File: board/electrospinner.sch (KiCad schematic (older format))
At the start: 40 parts, among them J1 12Vin, J2 Programmer, J3 MotorConnector, J4 TempSensor, J5 USB_B, SW1 ResetBTN, U1 TPS62147, U2 FT230XS, U3 MSP430G2553IPW20

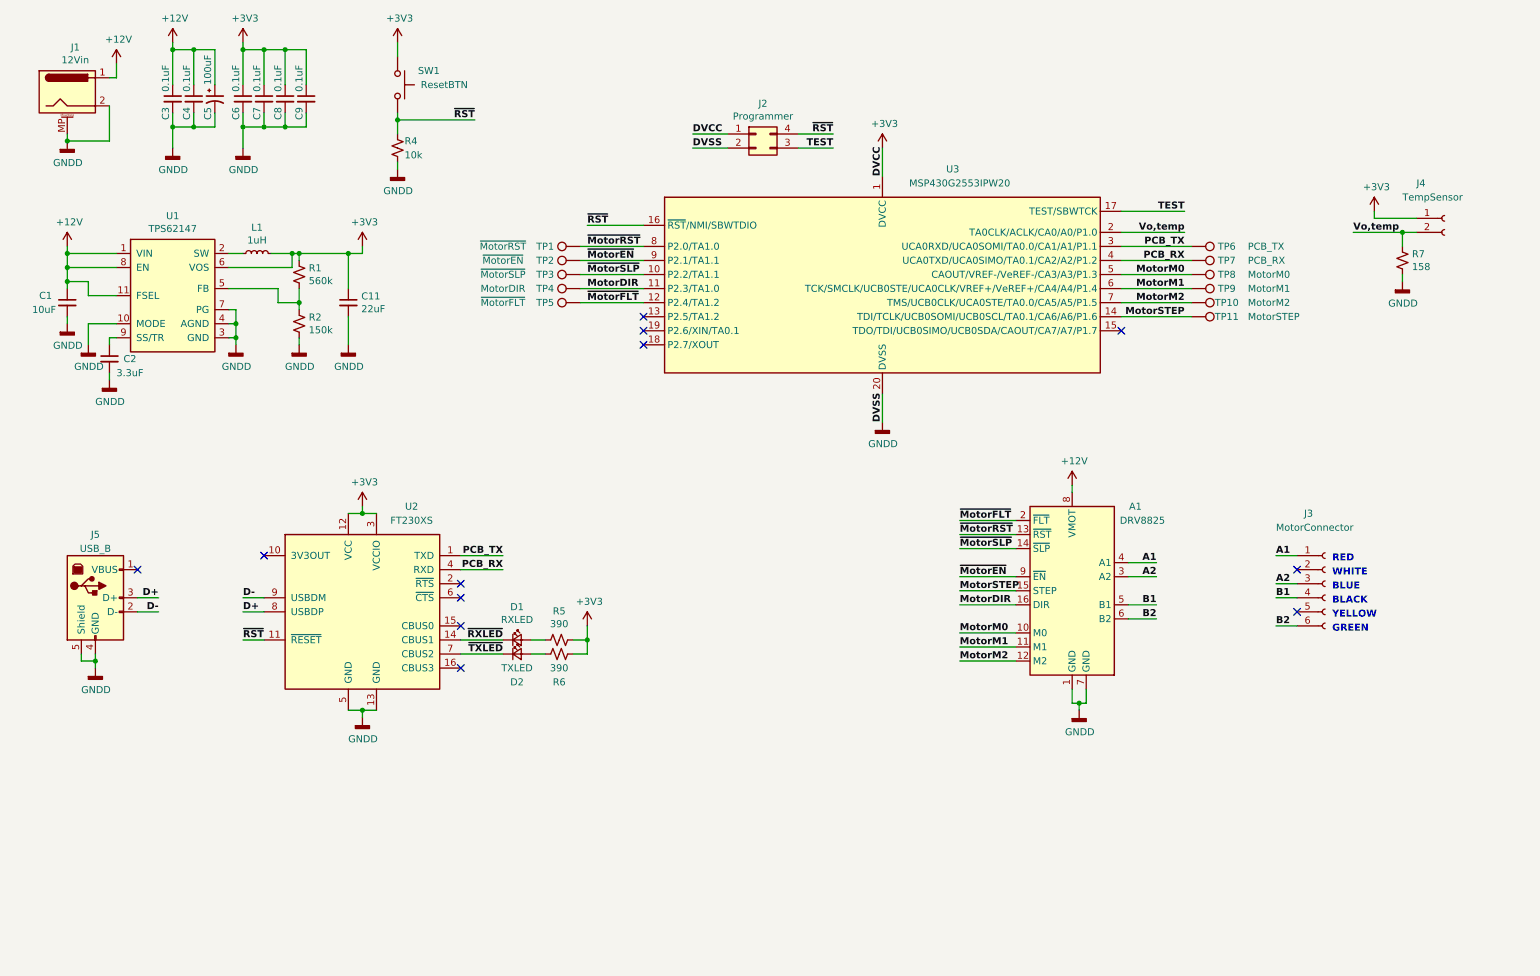
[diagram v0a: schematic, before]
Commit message: Re-updates rev5 files
Adds labels to schematic
Renames uart.pdf to usb_to_uart.pdf
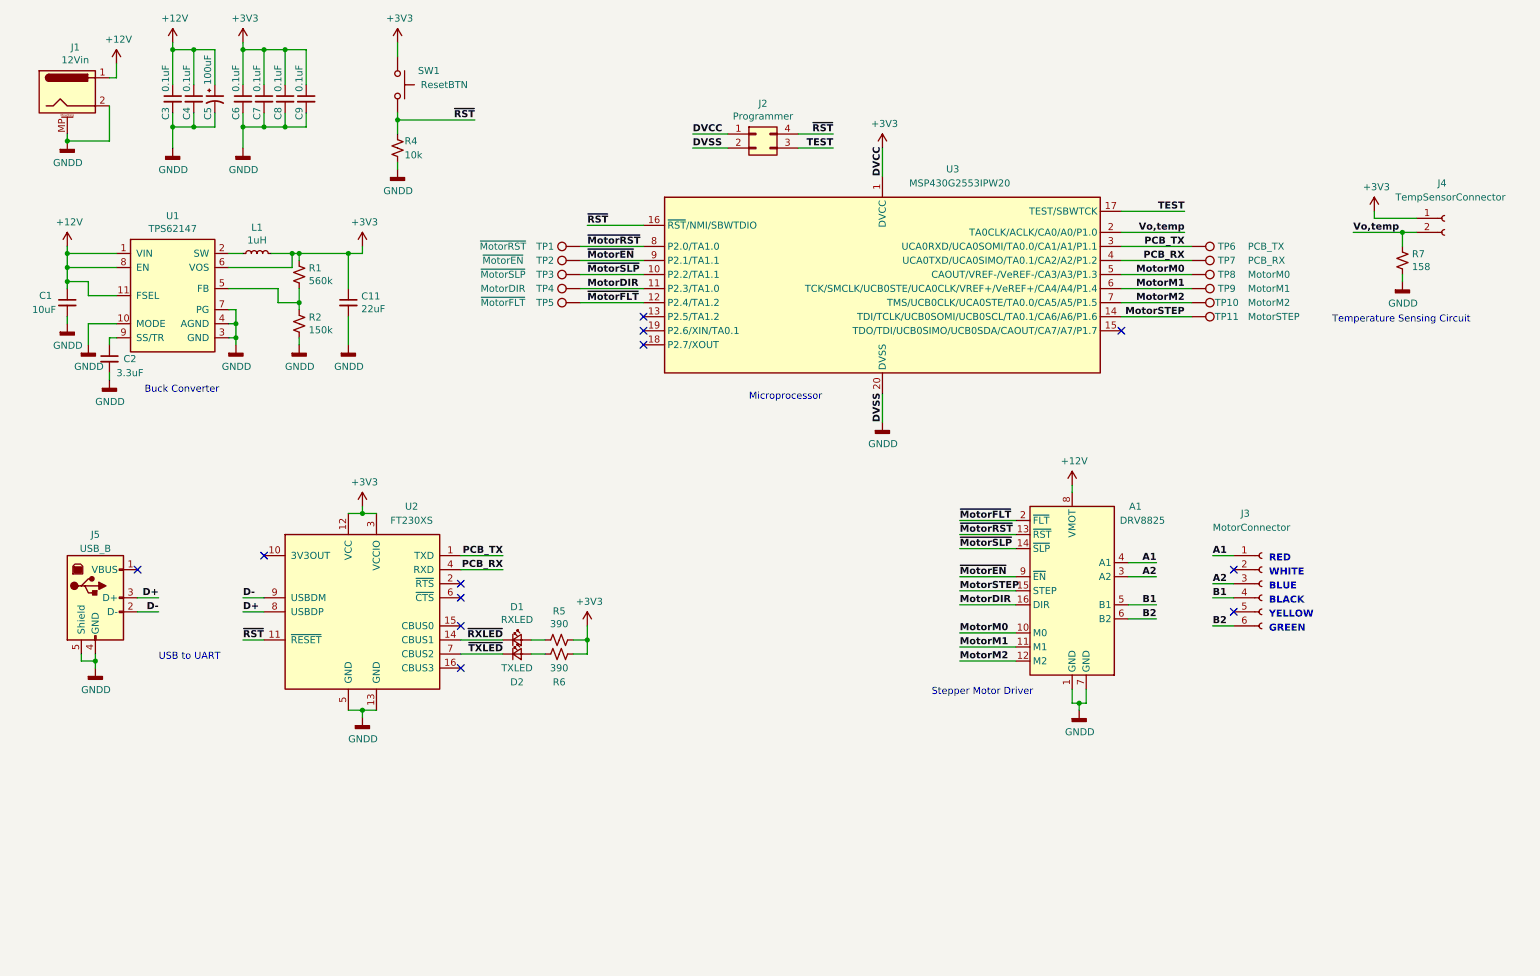
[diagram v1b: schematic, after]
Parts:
- J4: value TempSensor -> TempSensorConnector
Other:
- note added: "Buck Converter"
- note added: "Microprocessor"
- note added: "Stepper Motor Driver"
- note added: "Temperature Sensing Circuit"
- note added: "USB to UART"
- moved on the sheet: J3
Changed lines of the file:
@@
 L electrospinner-rescue:Conn_01x06_Female-Connector J3
 U 1 1 5C96304A
-P 9850 4550
-F 0 "J3" H 9700 5050 50  0000 L CNN
-F 1 "MotorConnector" H 9500 4950 50  0000 L CNN
-F 2 "Connector_JST:JST_XH_B6B-XH-AM_1x06_P2.50mm_Vertical" H 9850 4550 50  0001 C CNN
-F 3 "~" H 9850 4550 50  0001 C CNN
-F 4 "resource-center" H 2650 -850 50  0001 C CNN "Status"
-	1    9850 4550
-	1    0    0    -1
-$EndComp
-NoConn ~ 9650 4750
-NoConn ~ 9650 4450
-Text Label 9500 4850 0    50   ~ 10
+P 9400 4550
+F 0 "J3" H 9250 5050 50  0000 L CNN
+F 1 "MotorConnector" H 9050 4950 50  0000 L CNN
+F 2 "Connector_JST:JST_XH_B6B-XH-AM_1x06_P2.50mm_Vertical" H 9400 4550 50  0001 C CNN
+F 3 "~" H 9400 4550 50  0001 C CNN
+F 4 "resource-center" H 2200 -850 50  0001 C CNN "Status"
+	1    9400 4550
+	1    0    0    -1
+$EndComp
+NoConn ~ 9200 4750
+NoConn ~ 9200 4450
+Text Label 9050 4850 0    50   ~ 10
 B2
-Text Label 9500 4650 0    50   ~ 10
+Text Label 9050 4650 0    50   ~ 10
 B1
-Text Label 9500 4550 0    50   ~ 10
+Text Label 9050 4550 0    50   ~ 10
 A2
 Text Label 8850 2150 2    50   ~ 10
@@
 MotorDIR
 Wire Wire Line
-	9650 4850 9500 4850
-Wire Wire Line
-	9650 4650 9500 4650
-Wire Wire Line
-	9650 4550 9500 4550
-Wire Wire Line
-	9650 4350 9500 4350
+	9200 4850 9050 4850
+Wire Wire Line
+	9200 4650 9050 4650
+Wire Wire Line
+	9200 4550 9050 4550
+Wire Wire Line
+	9200 4350 9050 4350
 Text Label 4600 2000 0    50   ~ 10
 ~RST
@@
 	0    -1   -1   0
 $EndComp
-Text Notes 9900 4400 0    50   ~ 10
+Text Notes 9450 4400 0    50   ~ 10
 RED
-Text Notes 9900 4500 0    50   ~ 10
+Text Notes 9450 4500 0    50   ~ 10
 WHITE
-Text Label 9500 4350 0    50   ~ 10
+Text Label 9050 4350 0    50   ~ 10
 A1
-Text Notes 9900 4600 0    50   ~ 10
+Text Notes 9450 4600 0    50   ~ 10
 BLUE
-Text Notes 9900 4700 0    50   ~ 10
+Text Notes 9450 4700 0    50   ~ 10
 BLACK
-Text Notes 9900 4800 0    50   ~ 10
+Text Notes 9450 4800 0    50   ~ 10
 YELLOW
-Text Notes 9900 4900 0    50   ~ 10
+Text Notes 9450 4900 0    50   ~ 10
 GREEN
 Wire Wire Line
@@
 U 1 1 5C8E31D3
 P 10700 1950
-F 0 "J4" H 10500 2200 50  0000 L CNN
-F 1 "TempSensor" H 10400 2100 50  0000 L CNN
+F 0 "J4" H 10650 2200 50  0000 L CNN
+F 1 "TempSensorConnector" H 10350 2100 50  0000 L CNN
 F 2 "Connector_JST:JST_XH_B2B-XH-AM_1x02_P2.50mm_Vertical" H 10700 1950 50  0001 C CNN
 F 3 "~" H 10700 1950 50  0001 C CNN
@@
 Wire Wire Line
 	2150 2200 2050 2200
+Text Notes 1450 3200 0    50   ~ 0
+Buck Converter
+Text Notes 5750 3250 0    50   ~ 0
+Microprocessor
+Text Notes 1550 5100 0    50   ~ 0
+USB to UART
+Text Notes 7050 5350 0    50   ~ 0
+Stepper Motor Driver
+Text Notes 9900 2700 0    50   ~ 0
+Temperature Sensing Circuit
 $EndSCHEMATC

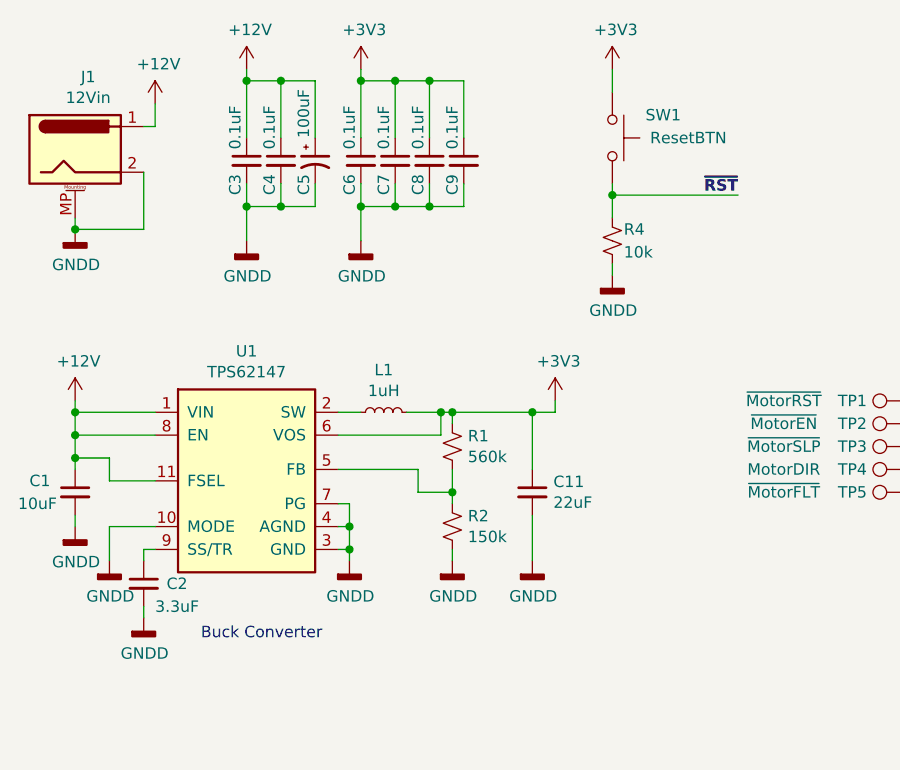
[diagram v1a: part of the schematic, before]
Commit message: Updates schematic for rev6
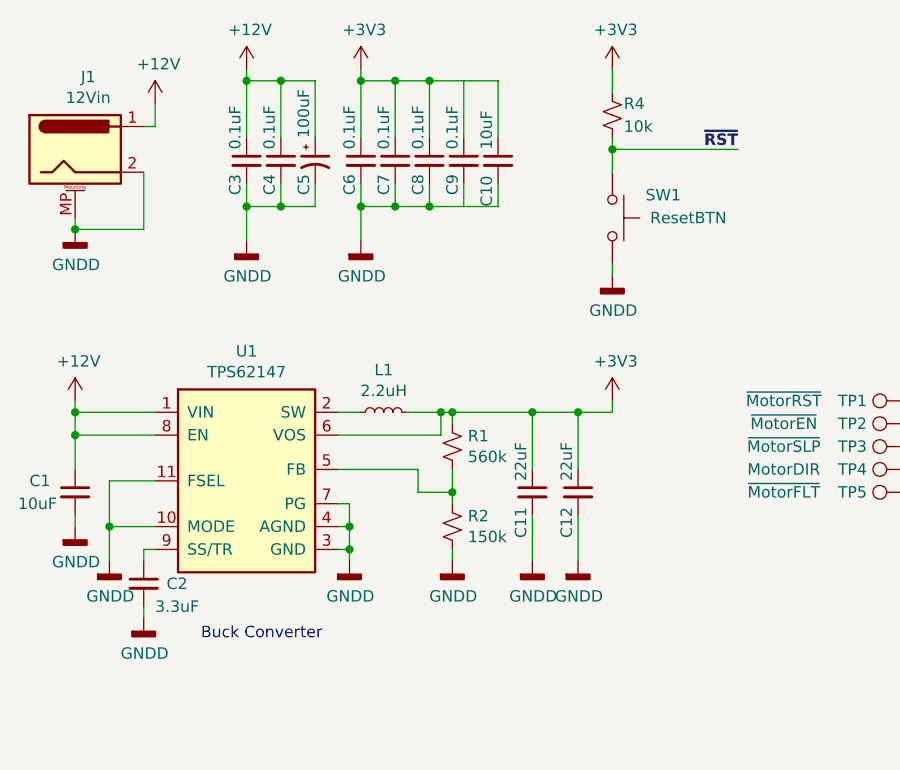
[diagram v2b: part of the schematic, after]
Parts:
- added C10: 10uF, Capacitor_SMD:C_0805_2012Metric, symbol Device:C_Small
- added C12: 22uF, Capacitor_SMD:C_0805_2012Metric, symbol electrospinner-rescue:C_Small-Device-electrospinner-rescue
- C1: Manufacturer (none) -> KEMET
- L1: value 1uH -> 2.2uH
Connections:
- net +12V: no longer U1.11 (FSEL)
- net +3V3: now also R4.1, C10.1, C12.1; no longer SW1.2
- net GNDD: now also SW1.1, U1.11 (FSEL), C10.2, C12.2; no longer R4.2
- net ~RST: now also R4.2, SW1.2; no longer R4.1, SW1.1
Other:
- moved on the sheet: R4, SW1
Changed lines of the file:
@@
 Sheet 1 1
 Title "Electrospinner PCB"
-Date "2019-04-09"
-Rev "5"
+Date "2019-04-11"
+Rev "6"
 Comp "PEDC"
 Comment1 ""
@@
 F 3 "https://www.mouser.com/datasheet/2/212/KEM_C1078_X7R_FT-CAP_AUTO_SMD-1103315.pdf" H 900 2550 50  0001 C CNN
 F 4 "C0805X106K8RACAUTO" H -700 -150 50  0001 C CNN "MPN"
+F 5 "KEMET" H 0   0   50  0001 C CNN "Manufacturer"
 	1    900  2550
 	1    0    0    -1
@@
 P 2250 2200
 F 0 "L1" V 2435 2200 50  0000 C CNN
-F 1 "1uH" V 2344 2200 50  0000 C CNN
+F 1 "2.2uH" V 2344 2200 50  0000 C CNN
 F 2 "Inductor_SMD:L_0805_2012Metric" H 2250 2200 50  0001 C CNN
 F 3 "https://www.mouser.com/datasheet/2/281/J(E)TE243A-9101-1324383.pdf" H 2250 2200 50  0001 C CNN
@@
 U 1 1 5C8E53D8
 P 2900 2550
-F 0 "C11" H 2992 2596 50  0000 L CNN
-F 1 "22uF" H 2992 2505 50  0000 L CNN
+F 0 "C11" V 2850 2350 50  0000 L CNN
+F 1 "22uF" V 2850 2600 50  0000 L CNN
 F 2 "Capacitor_SMD:C_0805_2012Metric" H 2900 2550 50  0001 C CNN
 F 3 "https://www.mouser.com/datasheet/2/212/KEM_C1006_X5R_SMD-1103249.pdf" H 2900 2550 50  0001 C CNN
@@
 L electrospinner-rescue:+3V3-power #PWR023
 U 1 1 5C8E5402
-P 3000 2150
-F 0 "#PWR023" H 3000 2000 50  0001 C CNN
-F 1 "+3V3" H 3015 2323 50  0000 C CNN
-F 2 "" H 3000 2150 50  0001 C CNN
-F 3 "" H 3000 2150 50  0001 C CNN
-	1    3000 2150
-	1    0    0    -1
-$EndComp
-Wire Wire Line
-	3000 2150 3000 2200
-Wire Wire Line
-	3000 2200 2900 2200
-Connection ~ 2900 2200
+P 3250 2150
+F 0 "#PWR023" H 3250 2000 50  0001 C CNN
+F 1 "+3V3" H 3265 2323 50  0000 C CNN
+F 2 "" H 3250 2150 50  0001 C CNN
+F 3 "" H 3250 2150 50  0001 C CNN
+	1    3250 2150
+	1    0    0    -1
+$EndComp
+Wire Wire Line
+	3250 2150 3250 2200
 Connection ~ 2550 2200
 Wire Wire Line
@@
 Wire Wire Line
 	4600 2000 5000 2000
-Text Label 3800 1250 2    50   ~ 10
+Text Label 3800 1050 2    50   ~ 10
 ~RST
 $Comp
@@
 	3250 1550 3250 1600
 Wire Wire Line
-	3250 1250 3250 1350
-Wire Wire Line
-	3250 1250 3800 1250
+	3250 1050 3250 1150
+Wire Wire Line
+	3250 1050 3800 1050
 $Comp
 L electrospinner-rescue:+3V3-power #PWR025
@@
 $EndComp
 Wire Wire Line
-	3250 1200 3250 1250
-Connection ~ 3250 1250
+	3250 1000 3250 1050
+Connection ~ 3250 1050
 $Comp
 L electrospinner-rescue:SW_Push-Switch SW1
 U 1 1 5CA1B3E2
-P 3250 1000
-F 0 "SW1" V 3350 1300 50  0000 R CNN
-F 1 "ResetBTN" V 3250 1500 50  0000 R CNN
-F 2 "Button_Switch_THT:SW_PUSH_6mm_H5mm" H 3250 1200 50  0001 C CNN
-F 3 "~" H 3250 1200 50  0001 C CNN
-F 4 "resource-center" H -1200 -750 50  0001 C CNN "Status"
-	1    3250 1000
+P 3250 1350
+F 0 "SW1" V 3350 1650 50  0000 R CNN
+F 1 "ResetBTN" V 3250 1850 50  0000 R CNN
+F 2 "Button_Switch_THT:SW_PUSH_6mm_H5mm" H 3250 1550 50  0001 C CNN
+F 3 "~" H 3250 1550 50  0001 C CNN
+F 4 "resource-center" H -1200 -400 50  0001 C CNN "Status"
+	1    3250 1350
 	0    1    -1   0
 $EndComp
@@
 Wire Wire Line
 	2300 1200 2300 1300
-Wire Wire Line
-	2600 1000 2600 750
-Wire Wire Line
-	2600 750  2450 750
-Connection ~ 2450 750
-Wire Wire Line
-	2600 1200 2600 1300
-Wire Wire Line
-	2600 1300 2450 1300
-Connection ~ 2450 1300
 $Comp
 L electrospinner-rescue:R_Small_US-Device R4
 U 1 1 5CA15E6A
-P 3250 1450
-F 0 "R4" H 3300 1500 50  0000 L CNN
-F 1 "10k" H 3300 1400 50  0000 L CNN
-F 2 "Resistor_SMD:R_0805_2012Metric" H 3250 1450 50  0001 C CNN
-F 3 "https://www.mouser.com/datasheet/2/219/SG73G-1316861.pdf" H 3250 1450 50  0001 C CNN
-F 4 " SG73G2ATTD1001D " H -1200 -650 50  0001 C CNN "MPN"
-	1    3250 1450
+P 3250 900
+F 0 "R4" H 3300 950 50  0000 L CNN
+F 1 "10k" H 3300 850 50  0000 L CNN
+F 2 "Resistor_SMD:R_0805_2012Metric" H 3250 900 50  0001 C CNN
+F 3 "https://www.mouser.com/datasheet/2/219/SG73G-1316861.pdf" H 3250 900 50  0001 C CNN
+F 4 " SG73G2ATTD1001D " H -1200 -1200 50  0001 C CNN "MPN"
+	1    3250 900
 	1    0    0    -1
 $EndComp
@@
 $EndComp
 $Comp
-L Device:C_Small C8
-U 1 1 5CF4CD0D
-P 2450 1100
-F 0 "C8" V 2400 950 50  0000 L CNN
-F 1 "0.1uF" V 2400 1150 50  0000 L CNN
-F 2 "Capacitor_SMD:C_0805_2012Metric" H 2450 1100 50  0001 C CNN
-F 3 "https://www.mouser.com/datasheet/2/447/yageodocoutput-1313910.pdf" H 2450 1100 50  0001 C CNN
-F 4 "AS0805KKX7R9BB104" H 550 50  50  0001 C CNN "MPN"
-F 5 "Yageo" H 550 50  50  0001 C CNN "Manufacturer"
-	1    2450 1100
-	1    0    0    -1
-$EndComp
-$Comp
-L Device:C_Small C9
-U 1 1 5CF52A5A
-P 2600 1100
-F 0 "C9" V 2550 950 50  0000 L CNN
-F 1 "0.1uF" V 2550 1150 50  0000 L CNN
-F 2 "Capacitor_SMD:C_0805_2012Metric" H 2600 1100 50  0001 C CNN
-F 3 "https://www.mouser.com/datasheet/2/447/yageodocoutput-1313910.pdf" H 2600 1100 50  0001 C CNN
-F 4 "AS0805KKX7R9BB104" H 700 50  50  0001 C CNN "MPN"
-F 5 "Yageo" H 700 50  50  0001 C CNN "Manufacturer"
-	1    2600 1100
-	1    0    0    -1
-$EndComp
-$Comp
 L power:GNDD #PWR0119
 U 1 1 5CF5F358
@@
 Wire Wire Line
 	900  2300 1250 2300
-Wire Wire Line
-	1050 2500 1050 2400
-Wire Wire Line
-	1050 2400 900  2400
-Wire Wire Line
-	900  2400 900  2300
 Connection ~ 900  2300
-Wire Wire Line
-	900  2450 900  2400
-Connection ~ 900  2400
 Wire Wire Line
 	2350 2200 2500 2200
@@
 Text Notes 9900 2700 0    50   ~ 0
 Temperature Sensing Circuit
+Wire Wire Line
+	900  2300 900  2450
+Wire Wire Line
+	1050 2500 1050 2700
+Connection ~ 1050 2700
+Connection ~ 2450 1300
+Connection ~ 2450 750
+$Comp
+L Device:C_Small C8
+U 1 1 5CF4CD0D
+P 2450 1100
+F 0 "C8" V 2400 950 50  0000 L CNN
+F 1 "0.1uF" V 2400 1150 50  0000 L CNN
+F 2 "Capacitor_SMD:C_0805_2012Metric" H 2450 1100 50  0001 C CNN
+F 3 "https://www.mouser.com/datasheet/2/447/yageodocoutput-1313910.pdf" H 2450 1100 50  0001 C CNN
+F 4 "AS0805KKX7R9BB104" H 550 50  50  0001 C CNN "MPN"
+F 5 "Yageo" H 550 50  50  0001 C CNN "Manufacturer"
+	1    2450 1100
+	1    0    0    -1
+$EndComp
+Wire Wire Line
+	2600 1300 2450 1300
+Wire Wire Line
+	2600 1200 2600 1300
+Wire Wire Line
+	2600 750  2450 750
+Wire Wire Line
+	2600 1000 2600 750
+$Comp
+L Device:C_Small C9
+U 1 1 5CF52A5A
+P 2600 1100
+F 0 "C9" V 2550 950 50  0000 L CNN
+F 1 "0.1uF" V 2550 1150 50  0000 L CNN
+F 2 "Capacitor_SMD:C_0805_2012Metric" H 2600 1100 50  0001 C CNN
+F 3 "https://www.mouser.com/datasheet/2/447/yageodocoutput-1313910.pdf" H 2600 1100 50  0001 C CNN
+F 4 "AS0805KKX7R9BB104" H 700 50  50  0001 C CNN "MPN"
+F 5 "Yageo" H 700 50  50  0001 C CNN "Manufacturer"
+	1    2600 1100
+	1    0    0    -1
+$EndComp
+Wire Wire Line
+	2750 1000 2750 750
+Wire Wire Line
+	2750 750  2600 750
+Wire Wire Line
+	2750 1200 2750 1300
+Wire Wire Line
+	2750 1300 2600 1300
+$Comp
+L Device:C_Small C10
+U 1 1 5CB04A47
+P 2750 1100
+F 0 "C10" V 2700 900 50  0000 L CNN
+F 1 "10uF" V 2700 1150 50  0000 L CNN
+F 2 "Capacitor_SMD:C_0805_2012Metric" H 2750 1100 50  0001 C CNN
+F 3 "https://www.mouser.com/datasheet/2/212/KEM_C1078_X7R_FT-CAP_AUTO_SMD-1103315.pdf" H 2750 1100 50  0001 C CNN
+F 4 "C0805X106K8RACAUTO" H 850 50  50  0001 C CNN "MPN"
+F 5 "KEMET" H 850 50  50  0001 C CNN "Manufacturer"
+	1    2750 1100
+	1    0    0    -1
+$EndComp
+$Comp
+L electrospinner-rescue:C_Small-Device-electrospinner-rescue C12
+U 1 1 5CB1BF3D
+P 3100 2550
+F 0 "C12" V 3050 2350 50  0000 L CNN
+F 1 "22uF" V 3050 2600 50  0000 L CNN
+F 2 "Capacitor_SMD:C_0805_2012Metric" H 3100 2550 50  0001 C CNN
+F 3 "https://www.mouser.com/datasheet/2/212/KEM_C1006_X5R_SMD-1103249.pdf" H 3100 2550 50  0001 C CNN
+F 4 "C0805C226M8PACTU" H -500 50  50  0001 C CNN "MPN"
+F 5 "KEMET" H 3100 2550 50  0001 C CNN "Manufacturer"
+	1    3100 2550
+	1    0    0    -1
+$EndComp
+Wire Wire Line
+	3100 2650 3100 2850
+Wire Wire Line
+	3100 2450 3100 2200
+$Comp
+L power:GNDD #PWR0122
+U 1 1 5CB1BF45
+P 3100 2850
+F 0 "#PWR0122" H 3100 2600 50  0001 C CNN
+F 1 "GNDD" H 3104 2695 50  0000 C CNN
+F 2 "" H 3100 2850 50  0001 C CNN
+F 3 "" H 3100 2850 50  0001 C CNN
+	1    3100 2850
+	1    0    0    -1
+$EndComp
+Wire Wire Line
+	2900 2200 3100 2200
+Connection ~ 2900 2200
+Connection ~ 3100 2200
+Wire Wire Line
+	3100 2200 3250 2200
 $EndSCHEMATC
